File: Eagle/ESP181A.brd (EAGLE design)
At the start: 38.6 x 25.1 mm, 30 parts

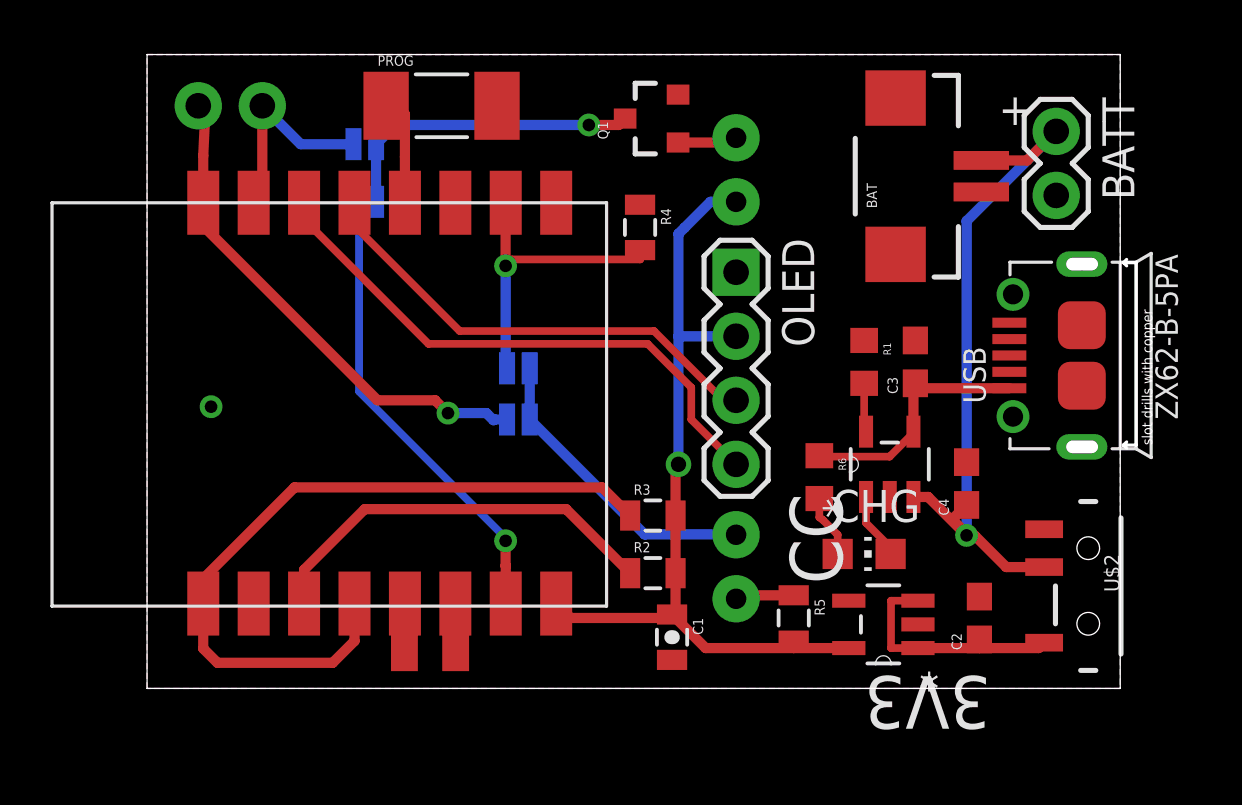
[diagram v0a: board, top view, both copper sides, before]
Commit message: Added battery voltage monitor
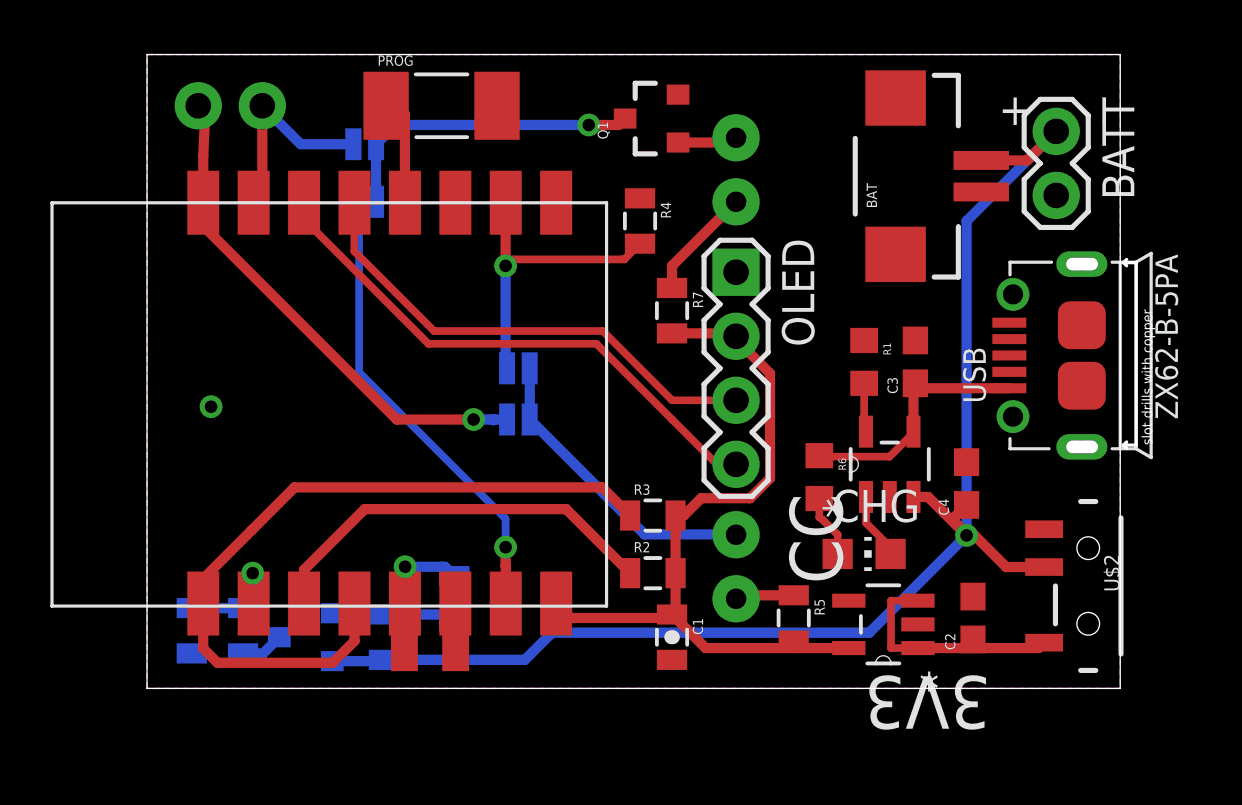
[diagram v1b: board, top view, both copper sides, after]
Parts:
- added C5: 0.1uF, SparkFun-Capacitors:0805-CAP
- added Q2: PFET, SparkFun-DiscreteSemi:SOT23-3
- added R10: 100K, SparkFun-Resistors:0805
- added R11: 2K2, SparkFun-Resistors:0805
- added R7: 47, SparkFun-Resistors:0805
- added R8: 10K, SparkFun-Resistors:0805
- moved C2 0.25 mm to (32.8, 2.79)
- moved R4 0.25 mm to (19.6, 18.5)
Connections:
- new net ADC: R10.1, R11.1, U$1.ADC
- new net N$11: P1.A, R7.1
- new net N$12: C5.2, Q2.1, R8.1
- new net N$13: Q2.3, R10.2
- net +5V: now also Q2.2, R8.2
- net 3V3: now also R7.2; no longer P1.A
- net GND: now also R11.2
- net IO14: now also C5.1
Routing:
- net +5V: track 29.0 -> 56.3 mm
- net ADC: track 0.00 -> 5.02 mm, vias 0 -> 1
- net N$12: track 0.00 -> 4.95 mm
- net N$11: track 0.00 -> 4.47 mm
- net IO14: track 1.60 -> 5.25 mm, vias 0 -> 1
- net 3V3: track 33.1 -> 29.9 mm, vias 1 -> 0
- net N$13: track 0.00 -> 1.71 mm
- net N$3: track 22.6 -> 21.8 mm
- net N$7: track 18.9 -> 19.5 mm
